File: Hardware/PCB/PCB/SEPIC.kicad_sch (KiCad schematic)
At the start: 16 parts, among them Q1 IRF7807, U1 LM3478MA

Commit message: Basic schematic
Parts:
- added D2, D3: Vin_syg, symbol Device:LED
- added R6, R7: 1k, symbol Device:R
- added TP1: Vout, Connector_Pin:Pin_D1.0mm_L10.0mm, symbol Connector:TestPoint
- added TP2: Vin, Connector_Pin:Pin_D1.0mm_L10.0mm, symbol Connector:TestPoint
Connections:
- net GND: now also R6.1, R7.1
- net Vin: now also D3.2 (A), TP2.1
- net Vout: now also D2.2 (A), TP1.1
- net Isen: now reaches C6.2, Q1.3 (S), R1.1, U1.1 (I_{SEN})
- net Isen: no longer R4.1, R5.2, U1.3 (FB)
- net DR: now reaches Q1.2 (G), U1.6 (DR)
- new net: D2.1 (K), R6.2
- new net: D3.1 (K), R7.2
- new net Feedback: R4.1, R5.2, U1.3 (FB)
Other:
- moved on the sheet: C1, C3, C4, C5, C6, C7, D1, L1, L2, Q1, R1, R2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

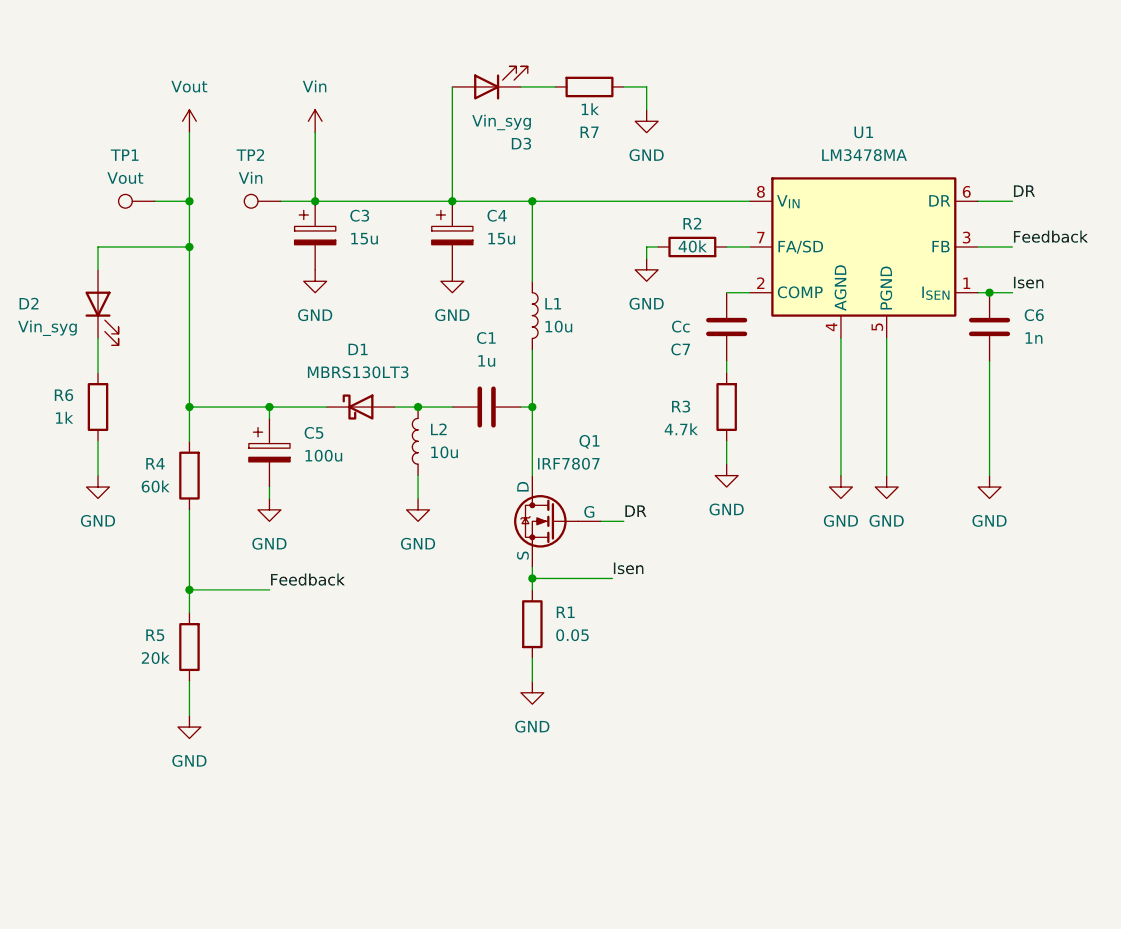
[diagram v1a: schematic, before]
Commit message: Update of PCB
After reading some of documentation, added capacitor on feedback lane and added potentiometer
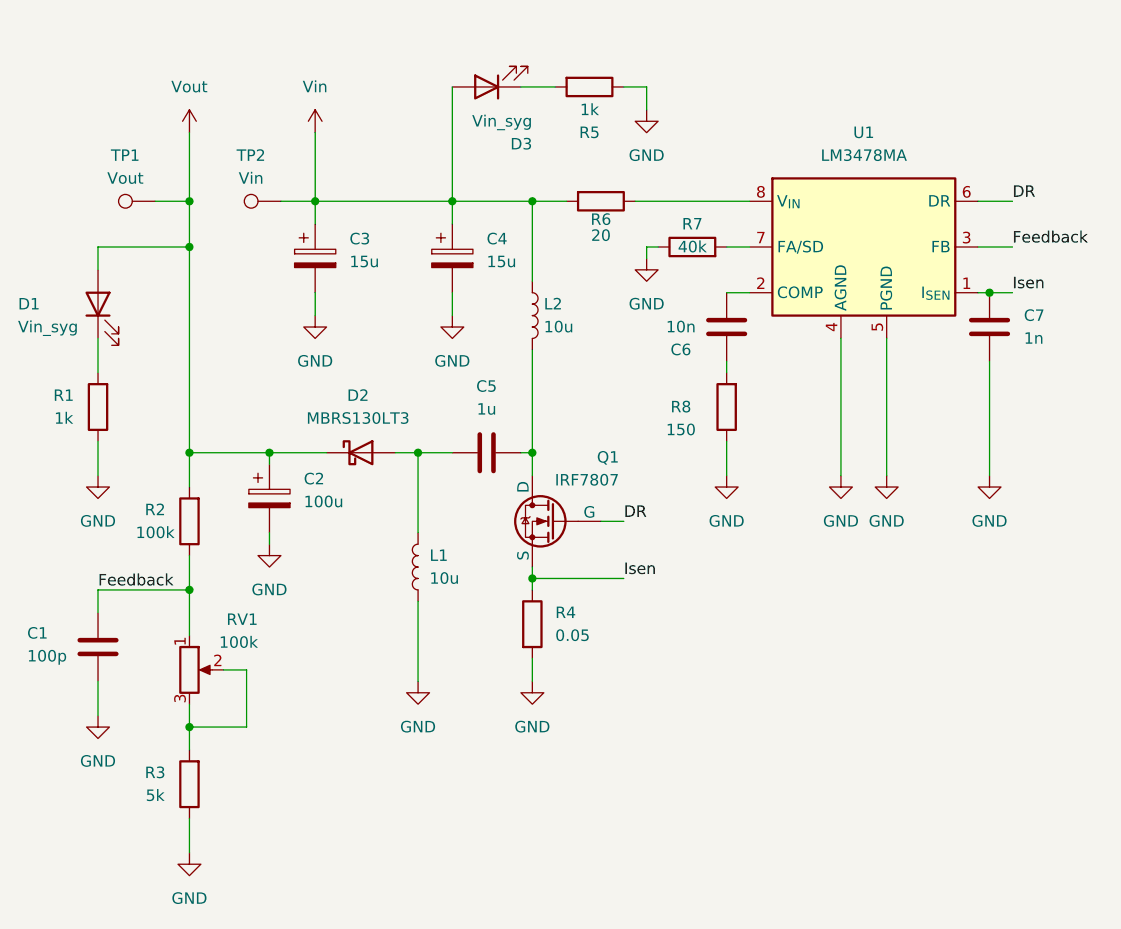
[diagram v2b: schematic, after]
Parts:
- added C1: 100p, Capacitor_SMD:C_1206_3216Metric, symbol Device:C
- added R6: 20, Resistor_SMD:R_1206_3216Metric, symbol Device:R
- added RV1: 100k, symbol Device:R_Potentiometer
- C5: renamed from C1; footprint (none) -> Capacitor_SMD:C_1206_3216Metric
- C6: renamed from C7; value Cc -> 10n; footprint (none) -> Capacitor_SMD:C_1206_3216Metric
- C7: renamed from C6; footprint (none) -> Capacitor_SMD:C_1206_3216Metric
- D1: renamed from D2; footprint (none) -> Resistor_SMD:R_1206_3216Metric
- D2: renamed from D1; footprint (none) -> Diode_SMD:D_1206_3216Metric
- D3: footprint (none) -> LED_SMD:LED_1206_3216Metric
- R1: renamed from R6; footprint (none) -> Resistor_SMD:R_1206_3216Metric
- R2: renamed from R4; value 60k -> 100k; footprint (none) -> Resistor_SMD:R_1206_3216Metric
- R3: renamed from R5; value 20k -> 5k; footprint (none) -> Resistor_SMD:R_1206_3216Metric
- R4: renamed from R1; footprint (none) -> Resistor_SMD:R_1206_3216Metric
- R5: renamed from R7; footprint (none) -> Resistor_SMD:R_1206_3216Metric
- R7: renamed from R2; footprint (none) -> Resistor_SMD:R_1206_3216Metric
- R8: renamed from R3; value 4.7k -> 150; footprint (none) -> Resistor_SMD:R_1206_3216Metric
- renumbered C5 to C2, L2 to L1, L1 to L2
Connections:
- net Feedback: now also C1.2, RV1.1; no longer R3.2
- net GND: now also C1.1
- net Vin: now also R6.2; no longer U1.8 (V_{IN})
- new net: R6.1, U1.8 (V_{IN})
- new net: R3.2, RV1.2, RV1.3
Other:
- company: (none) -> Bart Soul
- title: (none) -> SEPIC DC/DC Converter
- moved on the sheet: C2, C3, C4, C5, D2, L1, R2, R3
